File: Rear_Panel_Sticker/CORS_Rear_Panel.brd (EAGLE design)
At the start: 156.6 x 39 mm, 29 parts

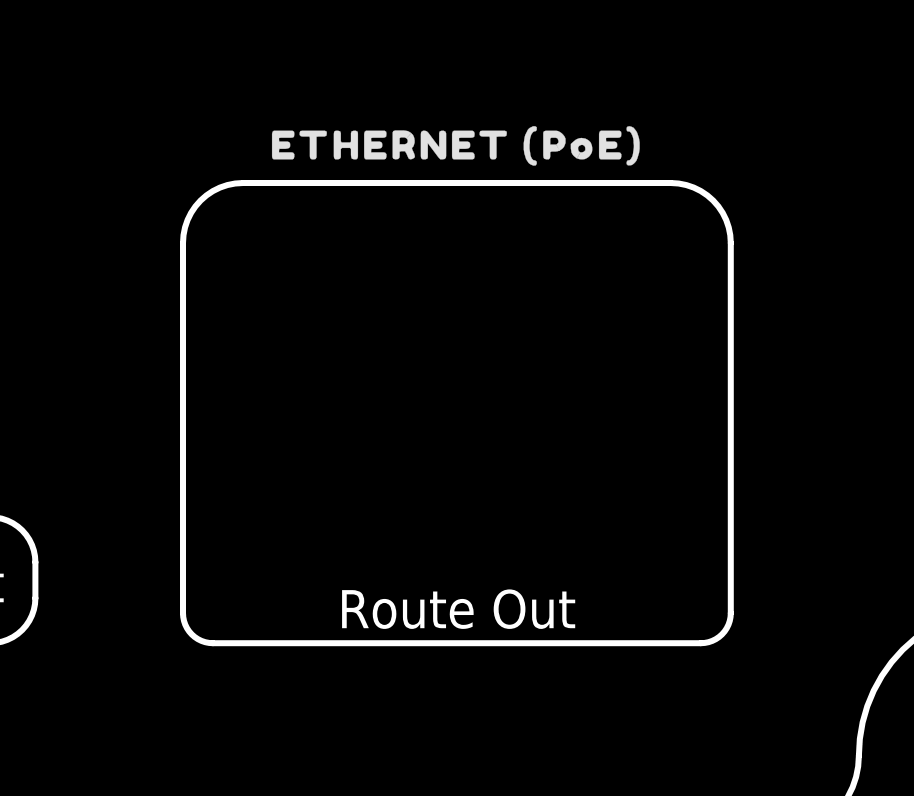
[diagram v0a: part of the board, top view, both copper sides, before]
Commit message: Update OLED and Ethernet
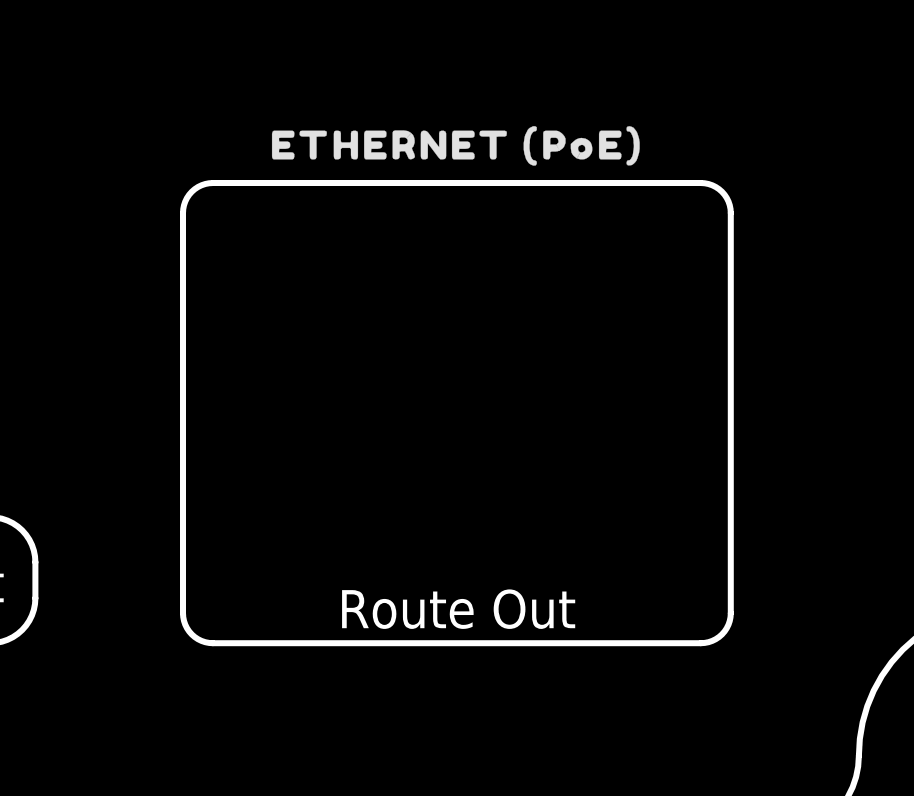
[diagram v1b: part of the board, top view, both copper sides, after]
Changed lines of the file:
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@@
 <drawing>
 <settings>
-<setting alwaysvectorfont="yes"/>
+<setting alwaysvectorfont="no"/>
 <setting verticaltext="up"/>
 </settings>

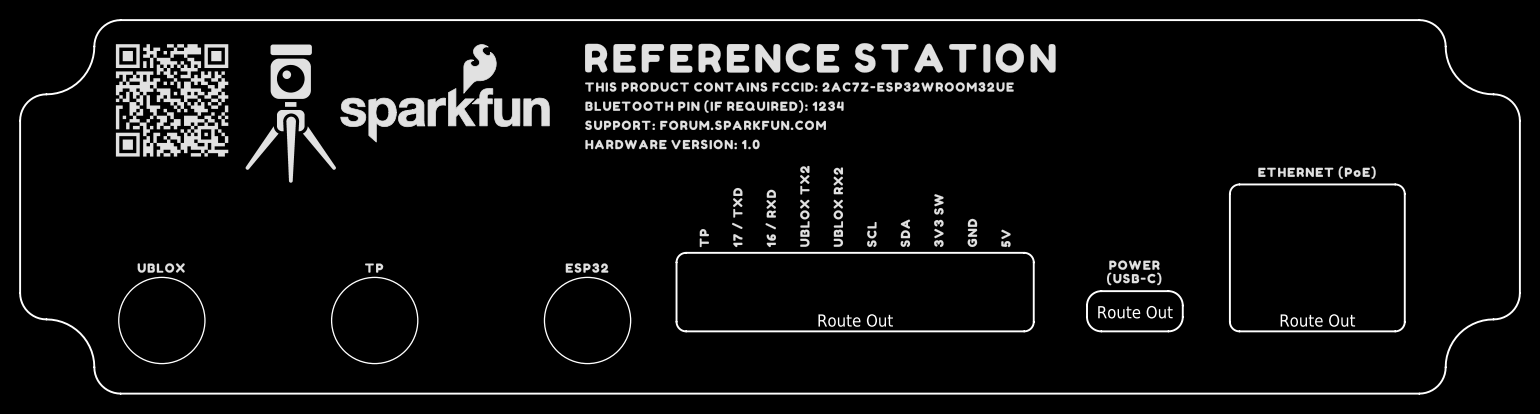
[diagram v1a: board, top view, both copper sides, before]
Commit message: Update stickers
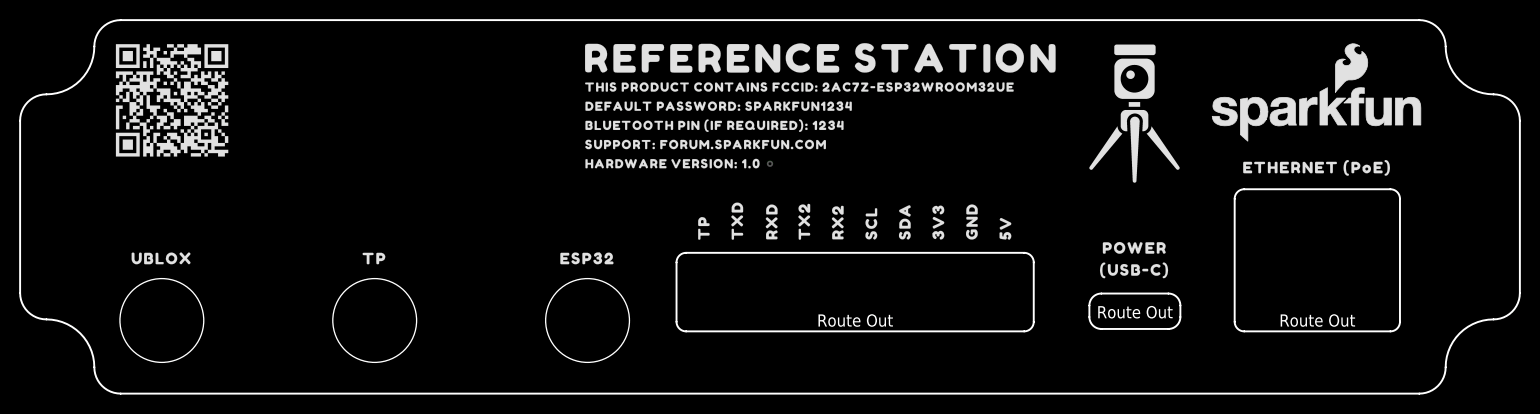
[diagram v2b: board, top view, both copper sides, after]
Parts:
- removed U$21: (no value), output:GND2222
- removed U$22: (no value), output:5V2223
- removed U$24: (no value), output:POWER0
- removed U$26: (no value), output:_##USB#C##_0
- removed U$27: (no value), output:ETHERNET_##POE##_0
- added U$23: (no value), output:UBLOX326
- added U$28: (no value), output:TP327
- added U$29: (no value), output:ESP324
- added U$40: (no value), output:POWER22335
- added U$41: (no value), output:_#USB#C#_22336
- added U$42: (no value), output:_ETHERNET_#POE#_22337
- U$10: device output:16_#_RXD18 -> output:TX23
- U$11: device output:TP0 -> output:RX224
- U$12: device output:TP1 -> output:SCL225
- U$16: device output:UBLOX_TX218 -> output:SDA226
- U$17: device output:UBLOX_RX2219 -> output:3V3227
- U$18: device output:SCL2220 -> output:GND227
- U$19: device output:SDA2221 -> output:5V228
- U$20: device output:3V3_SW2222 -> output:DEFAULT_PASSWORD#_SPARKFUN12340
- U$5: device output:ESP320 -> output:TP0
- U$6: device output:UBLOX0 -> output:TXD1
- U$9: device output:17_#_TXD0 -> output:RXD2
- moved LOGO1 91.0 mm to (57.1, 22.2)
- moved U$6 60.1 mm to (-3.40, 8.20), turned to 90 degrees
- moved U$11 48.4 mm to (7.10, 8.20), turned to 90 degrees
- moved U$20 40.7 mm to (-20.0, 23.0), turned to 0 degrees
- moved U$12 17.5 mm to (10.6, 8.20)
- moved U$5 12.3 mm to (-6.90, 8.20), turned to 90 degrees
- moved U$17 10.5 mm to (17.6, 8.20)
- moved U$18 10.5 mm to (21.1, 8.20)
- moved U$19 10.5 mm to (24.6, 8.20)
- moved U$16 10.5 mm to (14.1, 8.20)
- moved U$9 3.60 mm to (0.20, 8.20)
- moved U$10 3.50 mm to (3.60, 8.20)
- moved U$3 2.00 mm to (-20.0, 21.0)
- moved U$4 2.00 mm to (-20.0, 19.0)
- moved U$7 2.00 mm to (-20.0, 17.0)
